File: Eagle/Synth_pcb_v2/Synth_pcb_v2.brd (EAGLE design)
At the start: 121 x 57 mm, 76 parts, among them IC3 LM358N, IC4 LM358N, IC5 LM358N, IC6 LM358N, T1 BC547, T2 BC547, T3 BC547, T4 BC547, T5 BC547, T6 BC547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

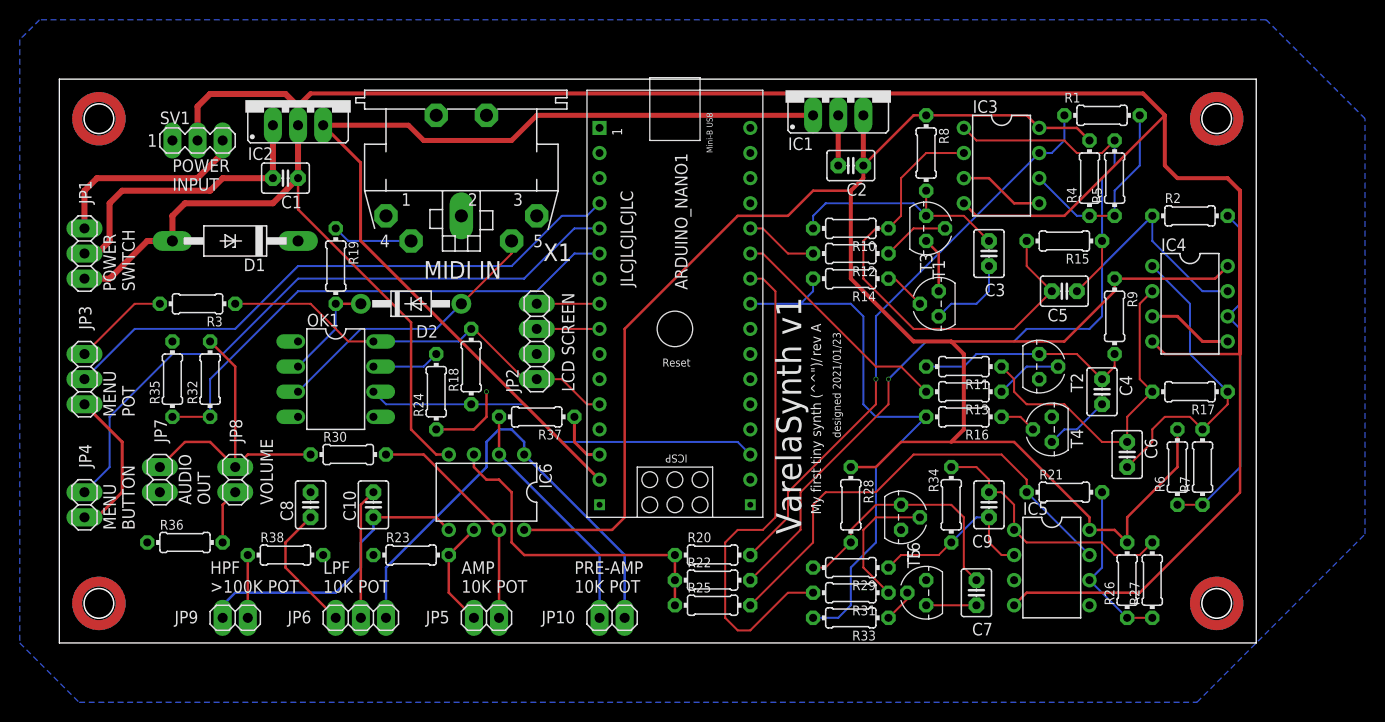
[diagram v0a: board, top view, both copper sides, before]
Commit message: Revision B made on time of manufacturing: corrected power schematic
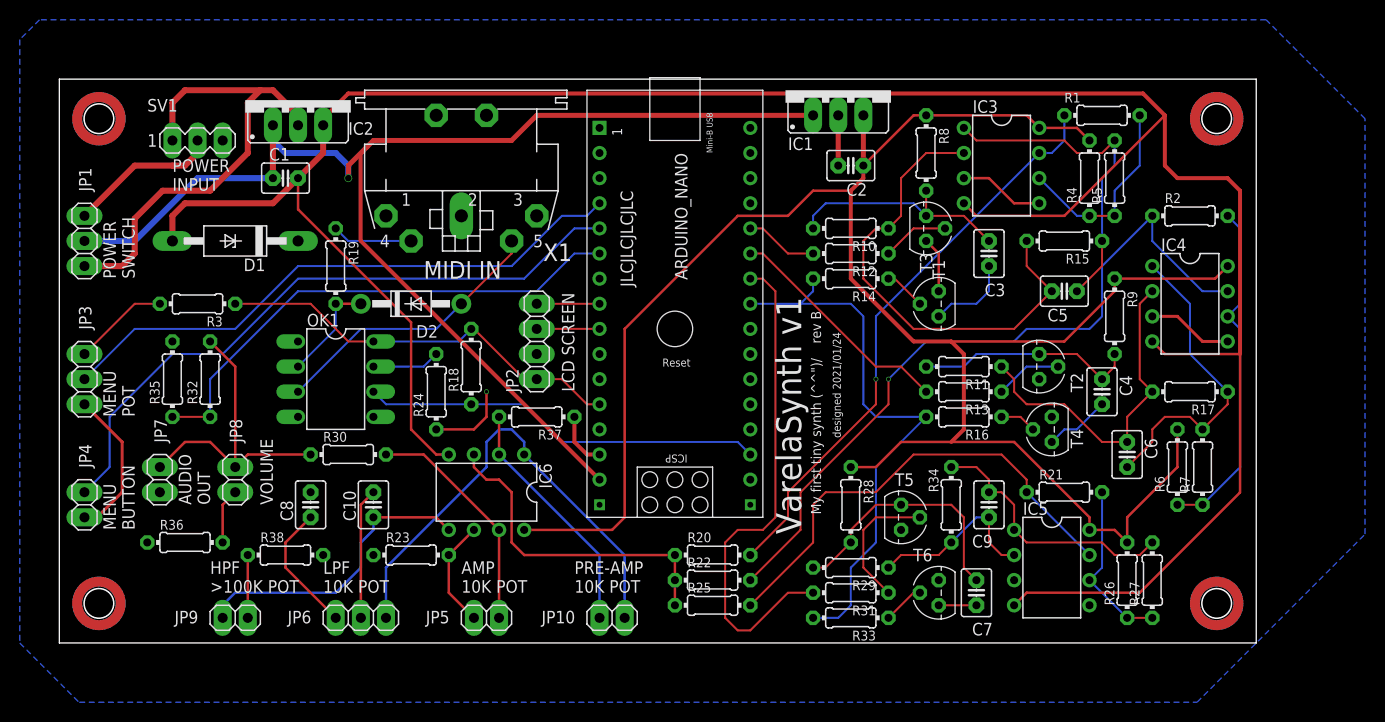
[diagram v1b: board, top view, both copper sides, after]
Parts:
- moved T6 1.27 mm to (88.9, 5.08)
- moved JP1 1.27 mm to (2.54, 40.6)
- turned C1 to 0 degrees
- renumbered ARDUINO_NANO1 to ARDUINO_NANO
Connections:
- removed net PWR: JP1.3, SV1.3
- new net 0V: IC2.IN, JP1.1, SV1.1
- net 0V_IN: now also C1.2, IC2.OUT; no longer C1.1, IC2.IN, JP1.1, SV1.2
- net 12V_IN: now also ARDUINO_NANO.15, C1.1, IC1.IN; no longer C1.2
- net V+: now also JP1.3, SV1.2; no longer ARDUINO_NANO.15, IC1.IN, IC2.OUT
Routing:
- net 12V_IN: track 29.8 -> 132.8 mm, vias 0 -> 1
- net V+: track 98.6 -> 15.3 mm
- net 0V: track 0.00 -> 49.3 mm
- net 0V_IN: track 281.4 -> 252.2 mm
- net PWR: track 20.6 -> 0.00 mm
- net N$41: track 5.08 -> 3.81 mm
- net N$48: track 3.33 -> 4.23 mm
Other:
- board text added: "designed 2021/01/24"
- board text added: "rev B"
- board text removed: "designed 2021/01/23"
- board text removed: "rev A"
